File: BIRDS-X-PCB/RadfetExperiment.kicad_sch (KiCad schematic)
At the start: 25 parts, among them U301 VT03, U302 VT03, U303 VT03, U304 VT03, U305 TL974IPWR, U306 ADG734, U307 LM335DT, U308 LM334M

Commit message: Update footprints to 0603
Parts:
- R301, R302, R303, R304, R305, R306, R307, R308, R309, R310, R311: footprint Resistor_SMD:R_0805_2012Metric_Pad1.20x1.40mm_HandSolder -> Resistor_SMD:R_0603_1608Metric_Pad0.98x0.95mm_HandSolder
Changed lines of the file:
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@@
       (effects (font (size 1.27 1.27)) (justify left))
     )
-    (property "Footprint" "Resistor_SMD:R_0805_2012Metric_Pad1.20x1.40mm_HandSolder" (at 210.566 66.294 90)
+    (property "Footprint" "Resistor_SMD:R_0603_1608Metric_Pad0.98x0.95mm_HandSolder" (at 210.566 66.294 90)
       (effects (font (size 1.27 1.27)) hide)
     )
@@
       (effects (font (size 1.27 1.27)) (justify left))
     )
-    (property "Footprint" "Resistor_SMD:R_0805_2012Metric_Pad1.20x1.40mm_HandSolder" (at 74.676 35.814 90)
+    (property "Footprint" "Resistor_SMD:R_0603_1608Metric_Pad0.98x0.95mm_HandSolder" (at 74.676 35.814 90)
       (effects (font (size 1.27 1.27)) hide)
     )
@@
       (effects (font (size 1.27 1.27)) (justify left))
     )
-    (property "Footprint" "Resistor_SMD:R_0805_2012Metric_Pad1.20x1.40mm_HandSolder" (at 63.246 35.814 90)
+    (property "Footprint" "Resistor_SMD:R_0603_1608Metric_Pad0.98x0.95mm_HandSolder" (at 63.246 35.814 90)
       (effects (font (size 1.27 1.27)) hide)
     )
@@
       (effects (font (size 1.27 1.27)) (justify left))
     )
-    (property "Footprint" "Resistor_SMD:R_0805_2012Metric_Pad1.20x1.40mm_HandSolder" (at 210.566 156.464 90)
+    (property "Footprint" "Resistor_SMD:R_0603_1608Metric_Pad0.98x0.95mm_HandSolder" (at 210.566 156.464 90)
       (effects (font (size 1.27 1.27)) hide)
     )
@@
       (effects (font (size 1.27 1.27)) (justify left))
     )
-    (property "Footprint" "Resistor_SMD:R_0805_2012Metric_Pad1.20x1.40mm_HandSolder" (at 210.566 90.424 90)
+    (property "Footprint" "Resistor_SMD:R_0603_1608Metric_Pad0.98x0.95mm_HandSolder" (at 210.566 90.424 90)
       (effects (font (size 1.27 1.27)) hide)
     )
@@
       (effects (font (size 1.27 1.27)) (justify left))
     )
-    (property "Footprint" "Resistor_SMD:R_0805_2012Metric_Pad1.20x1.40mm_HandSolder" (at 210.566 117.094 90)
+    (property "Footprint" "Resistor_SMD:R_0603_1608Metric_Pad0.98x0.95mm_HandSolder" (at 210.566 117.094 90)
       (effects (font (size 1.27 1.27)) hide)
     )
@@
       (effects (font (size 1.27 1.27)) (justify left))
     )
-    (property "Footprint" "Resistor_SMD:R_0805_2012Metric_Pad1.20x1.40mm_HandSolder" (at 210.566 100.584 90)
+    (property "Footprint" "Resistor_SMD:R_0603_1608Metric_Pad0.98x0.95mm_HandSolder" (at 210.566 100.584 90)
       (effects (font (size 1.27 1.27)) hide)
     )
@@
       (effects (font (size 1.27 1.27)) (justify left))
     )
-    (property "Footprint" "Resistor_SMD:R_0805_2012Metric_Pad1.20x1.40mm_HandSolder" (at 210.566 146.304 90)
+    (property "Footprint" "Resistor_SMD:R_0603_1608Metric_Pad0.98x0.95mm_HandSolder" (at 210.566 146.304 90)
       (effects (font (size 1.27 1.27)) hide)
     )
@@
       (effects (font (size 1.27 1.27)) (justify left))
     )
-    (property "Footprint" "Resistor_SMD:R_0805_2012Metric_Pad1.20x1.40mm_HandSolder" (at 210.566 127.254 90)
+    (property "Footprint" "Resistor_SMD:R_0603_1608Metric_Pad0.98x0.95mm_HandSolder" (at 210.566 127.254 90)
       (effects (font (size 1.27 1.27)) hide)
     )
@@
       (effects (font (size 1.27 1.27)) (justify left))
     )
-    (property "Footprint" "Resistor_SMD:R_0805_2012Metric_Pad1.20x1.40mm_HandSolder" (at 42.672 163.83 90)
+    (property "Footprint" "Resistor_SMD:R_0603_1608Metric_Pad0.98x0.95mm_HandSolder" (at 42.672 163.83 90)
       (effects (font (size 1.27 1.27)) hide)
     )
@@
       (effects (font (size 1.27 1.27)) (justify left))
     )
-    (property "Footprint" "Resistor_SMD:R_0805_2012Metric_Pad1.20x1.40mm_HandSolder" (at 210.566 76.454 90)
-      (effects (font (size 1.27 1.27)) hide)
-    )
+    (property "Footprint" "Resistor_SMD:R_0603_1608Metric_Pad0.98x0.95mm_HandSolder" (at 210.566 76.454 90)
+      (effects (font (size 1.27 1.27)) hide)
+    )

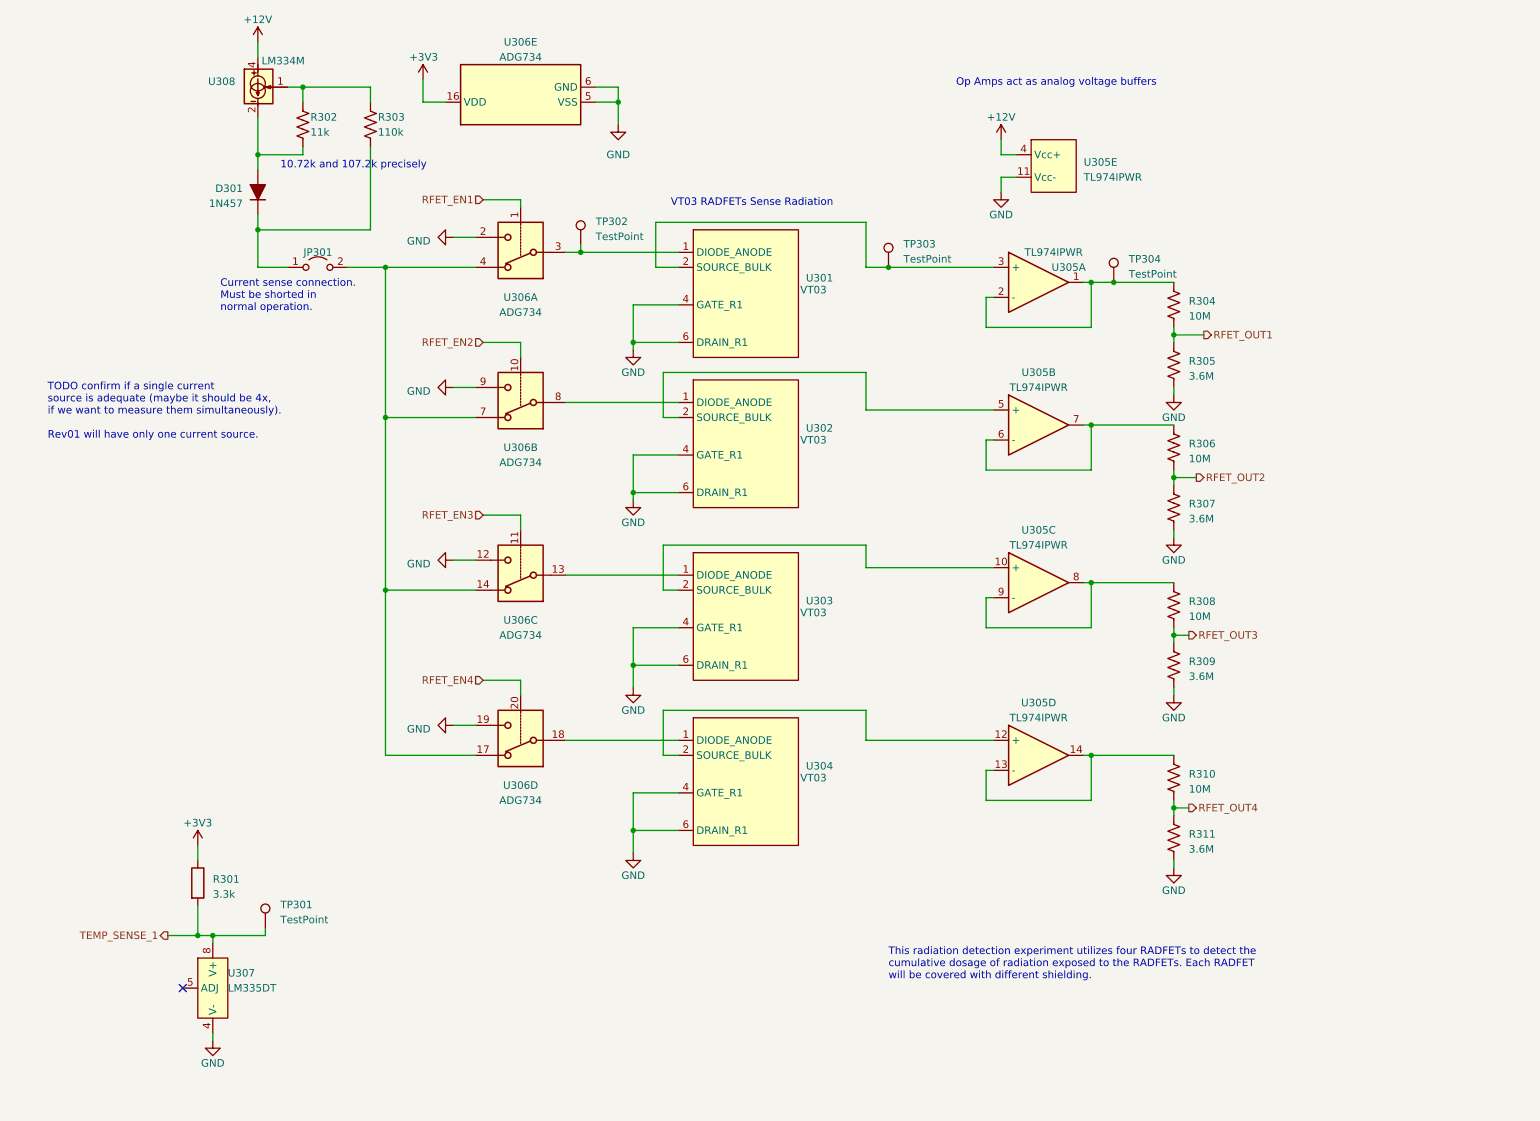
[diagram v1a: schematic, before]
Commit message: Do major layout
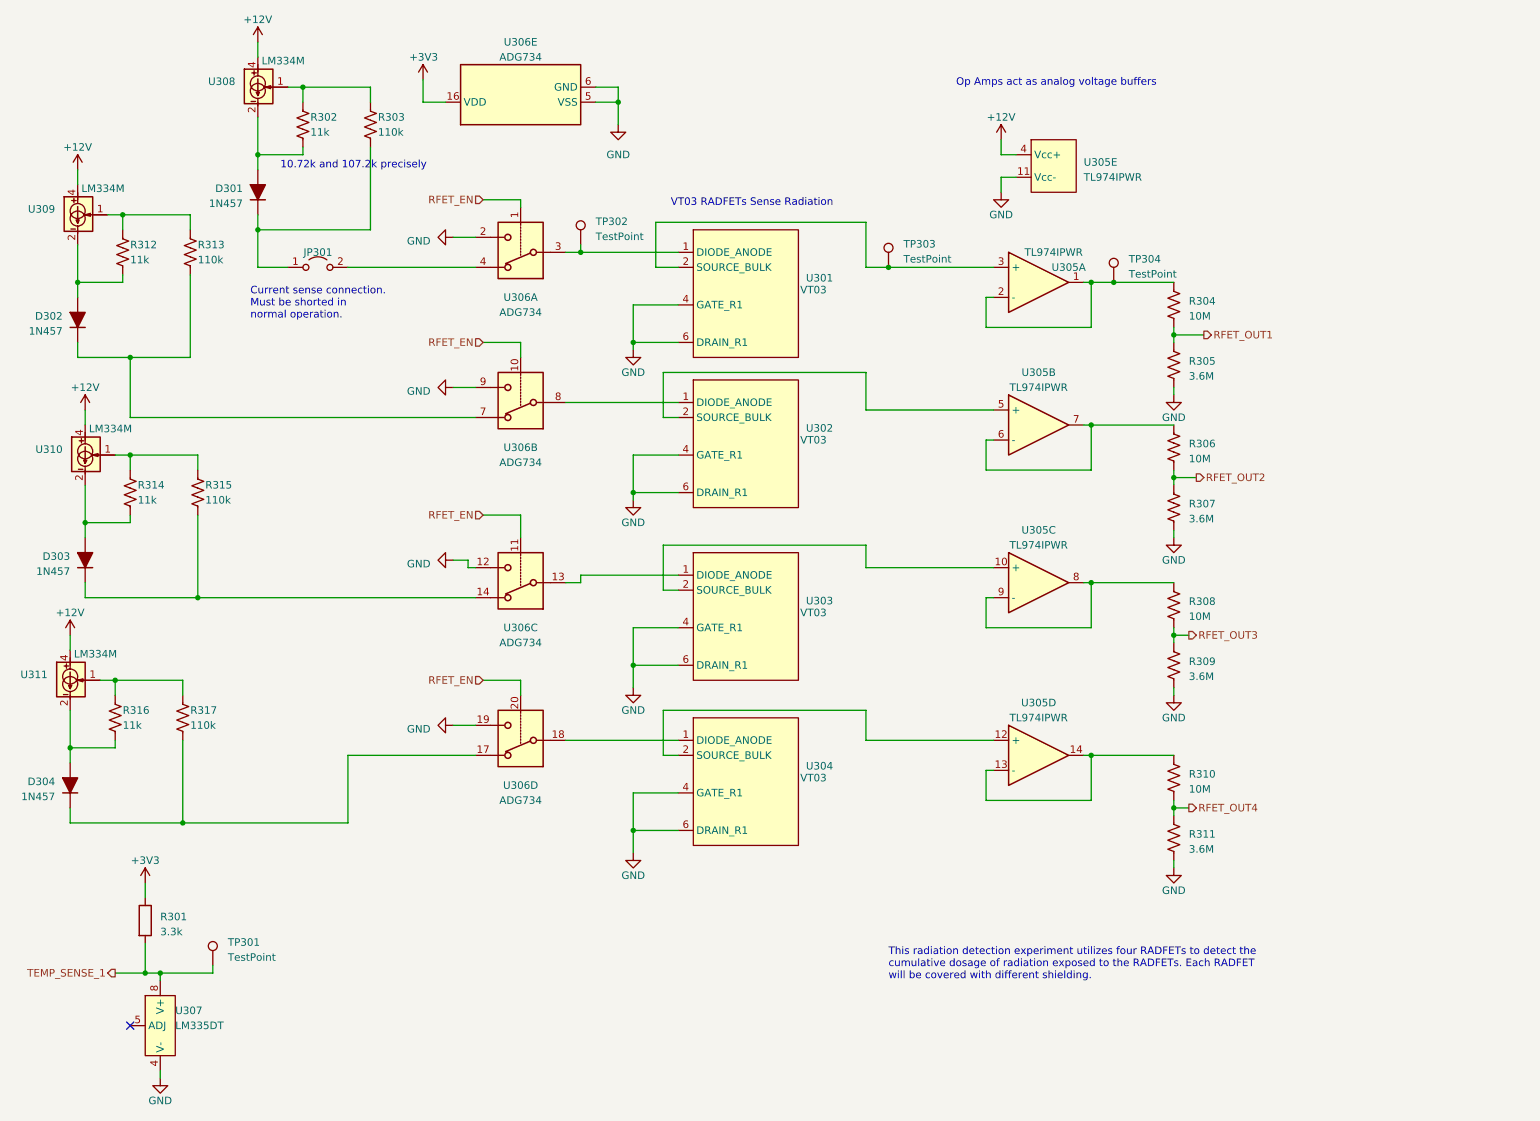
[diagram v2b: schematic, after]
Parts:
- added D302, D303, D304: 1N457, Diode_THT:D_DO-35_SOD27_P7.62mm_Horizontal, symbol BIRDS-X_Symbols_Lib:1N457
- added R312, R314, R316: 11k, Resistor_SMD:R_0603_1608Metric_Pad0.98x0.95mm_HandSolder, symbol Device:R_US
- added R313, R315, R317: 110k, Resistor_SMD:R_0603_1608Metric_Pad0.98x0.95mm_HandSolder, symbol Device:R_US
- added U309, U310, U311: LM334M, Package_SO:SOIC-8_3.9x4.9mm_P1.27mm, symbol BIRDS-X_Symbols_Lib:LM334M
- TP301, TP302, TP303, TP304: footprint TestPoint:TestPoint_Pad_D2.0mm -> TestPoint:TestPoint_Pad_D1.5mm
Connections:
- net RFET_EN2 is gone; now on net RFET_EN: U306.10
- net RFET_EN3 is gone; now on net RFET_EN: U306.11
- net RFET_EN4 is gone; now on net RFET_EN: U306.20
- net +12V: now also U309.4, U310.4, U311.4
- net RFET_EN1 renamed RFET_EN
- new net: R312.1, R313.1, U309.1
- new net: D302.2 (A), R312.2, U309.2, U309.3, U309.6, U309.7
- new net: R314.1, R315.1, U310.1
- new net: D303.1 (K), R315.2, U306.14
- new net: D303.2 (A), R314.2, U310.2, U310.3, U310.6, U310.7
- new net: R316.1, R317.1, U311.1
- new net: D304.2 (A), R316.2, U311.2, U311.3, U311.6, U311.7
- new net: D304.1 (K), R317.2, U306.17
- new net: JP301.2 (B), U306.4
- new net: D302.1 (K), R313.2, U306.7
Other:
- note removed: "TODO confirm if a single current source is adequate (maybe it should be 4x, if we want to measure them simultaneously). Rev01 will have only one current source."
- moved on the sheet: R301, TP301, U306C, U307

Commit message: Add MCU assignments, RF annotations per ref design, heirarchal pins
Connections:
- net RFET_OUT1 renamed RFET_SENSE_1
- net RFET_OUT2 renamed RFET_SENSE_2
- net RFET_OUT3 renamed RFET_SENSE_3
- net RFET_OUT4 renamed RFET_SENSE_4
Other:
- note added: "TODO add mounting holes"
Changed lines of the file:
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@@
+    (effects (font (size 1.27 1.27)) (justify left bottom))
+  )
+  (text "TODO add mounting holes" (at 101.6 182.88 0)
     (effects (font (size 1.27 1.27)) (justify left bottom))
   )
@@
     (effects (font (size 1.27 1.27)) (justify right))
   )
-  (hierarchical_label "RFET_OUT4" (shape output) (at 212.09 151.13 0) (fields_autoplaced)
+  (hierarchical_label "RFET_SENSE_4" (shape output) (at 212.09 151.13 0) (fields_autoplaced)
     (effects (font (size 1.27 1.27)) (justify left))
   )
-  (hierarchical_label "RFET_OUT1" (shape output) (at 214.63 71.12 0) (fields_autoplaced)
+  (hierarchical_label "RFET_SENSE_1" (shape output) (at 214.63 71.12 0) (fields_autoplaced)
     (effects (font (size 1.27 1.27)) (justify left))
   )
@@
     (effects (font (size 1.27 1.27)) (justify right))
   )
-  (hierarchical_label "RFET_OUT2" (shape output) (at 213.36 95.25 0) (fields_autoplaced)
+  (hierarchical_label "RFET_SENSE_2" (shape output) (at 213.36 95.25 0) (fields_autoplaced)
     (effects (font (size 1.27 1.27)) (justify left))
   )
-  (hierarchical_label "RFET_OUT3" (shape output) (at 212.09 121.92 0) (fields_autoplaced)
+  (hierarchical_label "RFET_SENSE_3" (shape output) (at 212.09 121.92 0) (fields_autoplaced)
     (effects (font (size 1.27 1.27)) (justify left))
   )

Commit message: Move around silkscreens for final production
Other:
- note added: "Bottom-Left - 4"
- note added: "Bottom-Right - 3"
- note added: "Top-Left - 1"
- note added: "Top-Right - 2"
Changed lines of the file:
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@@
     (stroke (width 0) (type default))
+  )
+  (text "Top-Right - 2" (at 231.14 102.87 0)
+    (effects (font (size 2.54 2.54) (thickness 0.508) bold) (justify left bottom))
+  )
+  (text "Bottom-Right - 3" (at 226.06 129.54 0)
+    (effects (font (size 2.54 2.54) (thickness 0.508) bold) (justify left bottom))
+  )
+  (text "Top-Left - 1" (at 232.41 77.47 0)
+    (effects (font (size 2.54 2.54) (thickness 0.508) bold) (justify left bottom))
   )
   (text "VT03 RADFETs Sense Radiation" (at 124.46 49.53 0)
@@
     (effects (font (size 1.27 1.27)) (justify left bottom))
   )
+  (text "Bottom-Left - 4" (at 227.33 146.05 0)
+    (effects (font (size 2.54 2.54) (thickness 0.508) bold) (justify left bottom))
+  )
   (text "Current sense connection.\nMust be shorted in\nnormal operation."

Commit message: Add LCSC LM334 part number for next time, remove point-in-time files
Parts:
- U308, U309, U310, U311: LCSC (none) -> C140388
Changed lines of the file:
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@@
       (effects (font (size 1.27 1.27) italic) hide)
+    )
+    (property "LCSC" "C140388" (at 54.61 29.21 0)
+      (effects (font (size 1.27 1.27)) hide)
     )
     (pin "1")
@@
       (effects (font (size 1.27 1.27) italic) hide)
     )
+    (property "LCSC" "C140388" (at 25.4 91.44 0)
+      (effects (font (size 1.27 1.27)) hide)
+    )
     (pin "1")
     (pin "2")
@@
     (property "Datasheet" "http://www.ti.com/lit/ds/symlink/lm134.pdf" (at 22.86 129.54 0)
       (effects (font (size 1.27 1.27) italic) hide)
+    )
+    (property "LCSC" "C140388" (at 22.86 129.54 0)
+      (effects (font (size 1.27 1.27)) hide)
     )
     (pin "1")
@@
       (effects (font (size 1.27 1.27) italic) hide)
     )
-    (pin "1")
+    (property "LCSC" "C140388" (at 24.13 50.8 0)
+      (effects (font (size 1.27 1.27)) hide)
+    )
+    (pin "1")
